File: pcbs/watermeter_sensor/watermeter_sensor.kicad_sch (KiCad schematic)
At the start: 14 parts, among them J1 Conn_01x06, U1 LDC2112, U2 MCP1811A

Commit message: Add Zigbee Microcontroller design files
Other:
- title: Water mater sensor -> Smart Water Meter Sensor
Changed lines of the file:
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@@
   (paper "A4")
   (title_block
-    (title "Water mater sensor")
+    (title "Smart Water Meter Sensor")
     (date "2021-11-07")
     (rev "1.0.0")

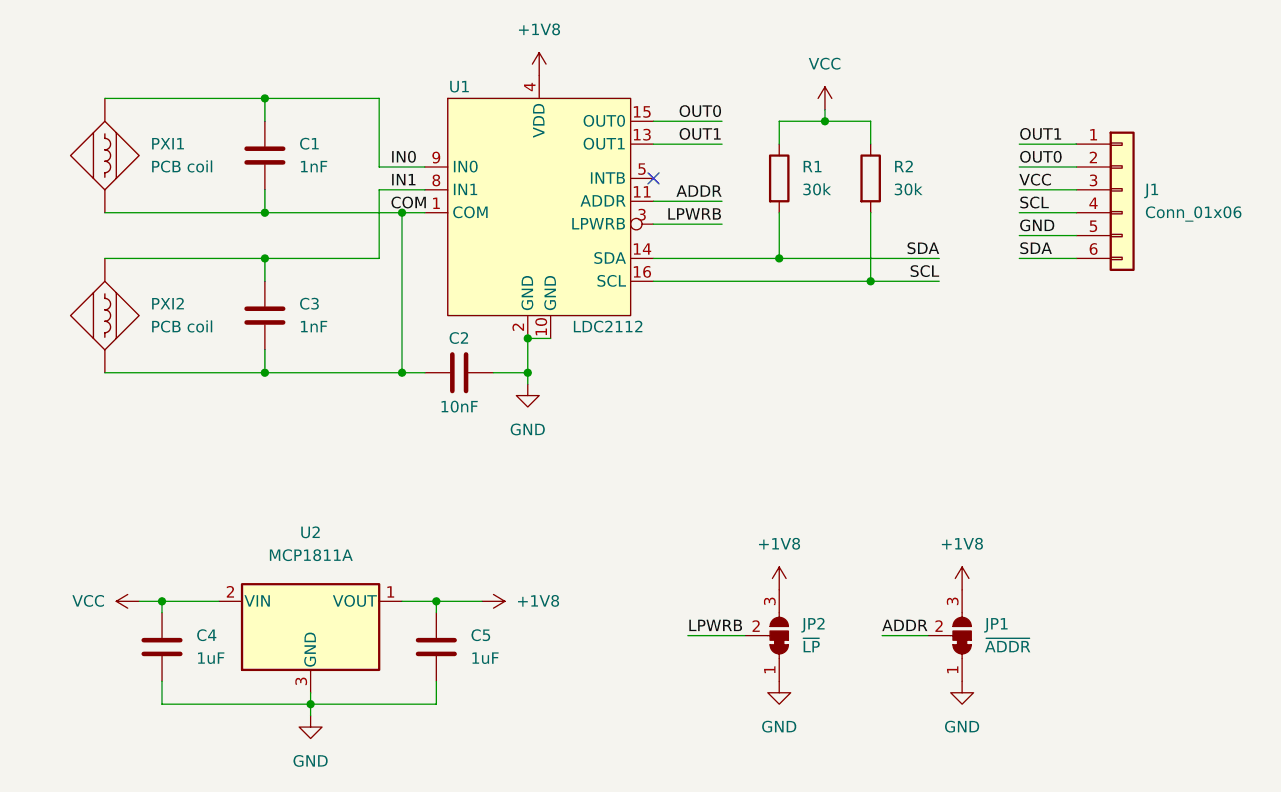
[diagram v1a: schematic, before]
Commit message: Watermeter v1.1 (#6)
* Update Arduino library
* PCB Changes v1.1:
- changed LDO
- some footprints changed to 0603
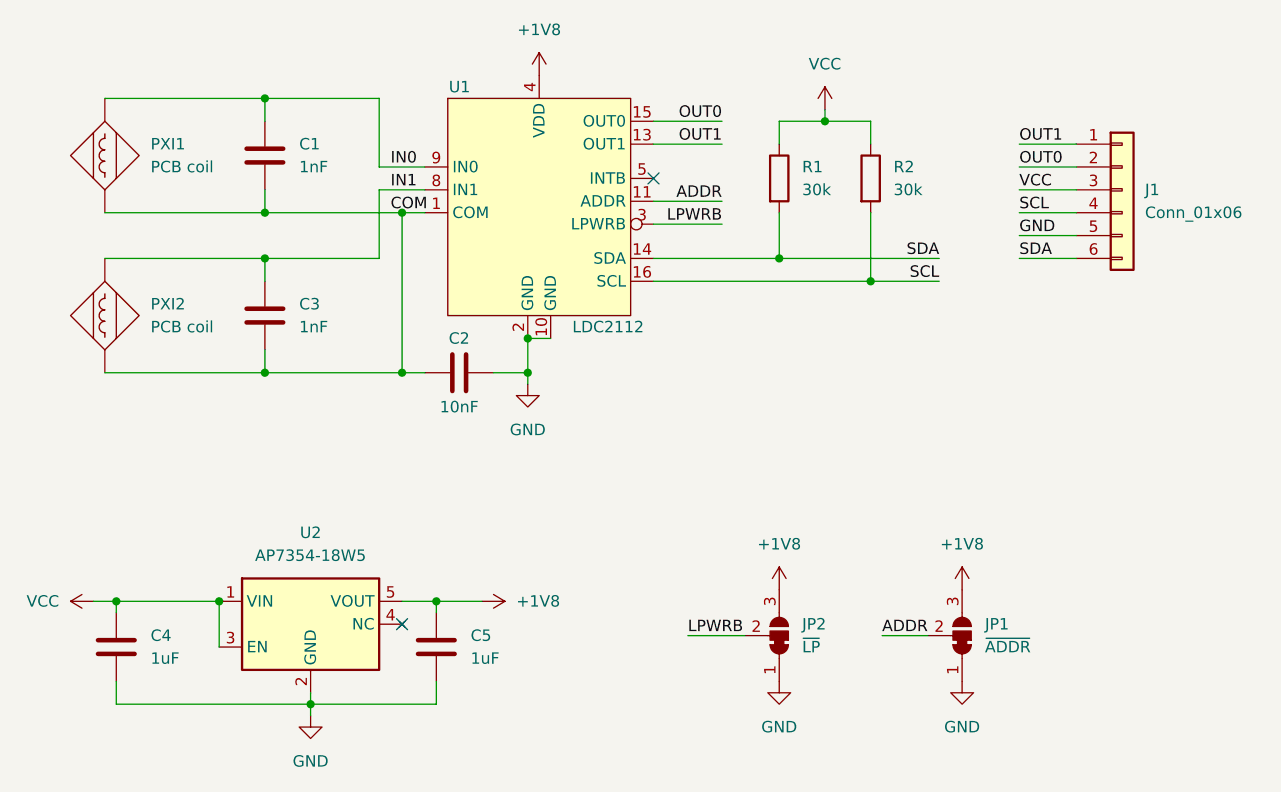
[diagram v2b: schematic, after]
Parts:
- removed U2: MCP1811A, Package_TO_SOT_SMD:SOT-23, symbol Regulator_Linear_Goodies:MCP1811A
- added U2: AP7354-18W5, Package_TO_SOT_SMD:TSOT-23-5, symbol Regulator_Linear:ADP7142AUJZ-1.8
- C1, C3: BOM (none) -> C0G 5% 50V
- C4: footprint Capacitor_SMD:C_0805_2012Metric -> Capacitor_SMD:C_0603_1608Metric
- C5: footprint Capacitor_SMD:C_0805_2012Metric -> Capacitor_SMD:C_0603_1608Metric; BOM (none) -> X7R 10% 6.3V
- PXI1, PXI2: Spice_Model 1uH -> (none); Spice_Netlist_Enabled Y -> (none); Spice_Primitive L -> (none)
- R1, R2: footprint Resistor_SMD:R_0805_2012Metric -> Resistor_SMD:R_0603_1608Metric
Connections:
- net +1V8: now also U2.5 (VOUT)
- net GND: now also U2.2 (GND)
- net VCC: now also U2.1 (VIN), U2.3 (EN)
- no-connect marks 1 -> 2
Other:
- moved on the sheet: C4
